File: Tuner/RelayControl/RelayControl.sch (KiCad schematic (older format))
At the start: 90 parts, among them J1 Conn_01x06, J12 Conn_01x01, J13 Conn_01x01, J14 Conn_01x01, J2 Conn_02x16_Odd_Even, J7 Conn_01x01, U1 MCP23017, U2 ULN2803A, U3 ULN2803A

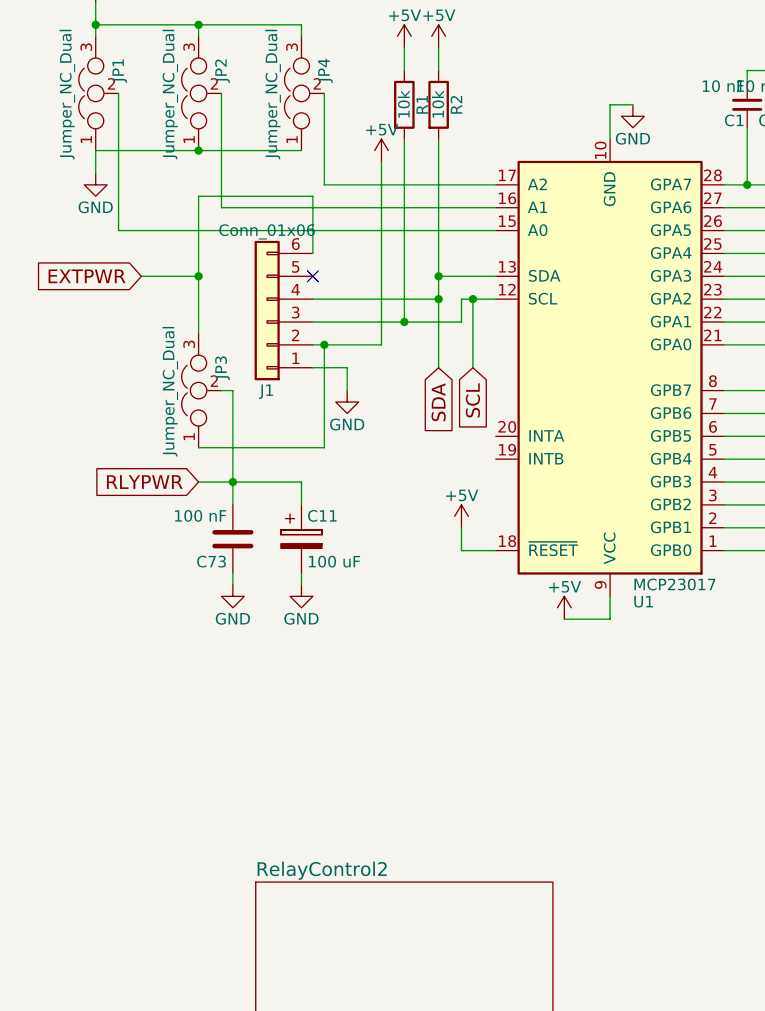
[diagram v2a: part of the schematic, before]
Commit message: JLCPCB order 09232018 - improved grounding - improved I2C cabling - NEO7M port - support for common mode chokes - relay board now has capacitors on all coils
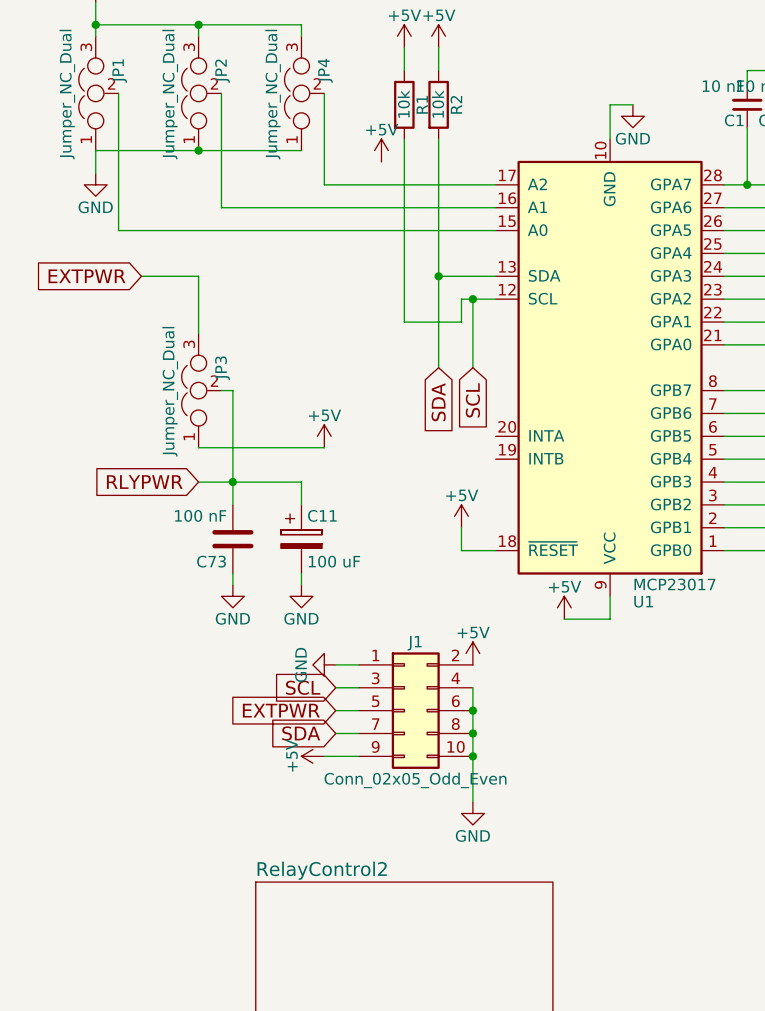
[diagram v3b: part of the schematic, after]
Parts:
- removed J1: Conn_01x06, Connectors_Molex:Molex_KK-6410-06_06x2.54mm_Straight, symbol Conn_01x06
- added J1: Conn_02x05_Odd_Even, Pin_Headers:Pin_Header_Straight_2x05_Pitch2.54mm, symbol Conn_02x05_Odd_Even
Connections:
- net +5V: now also J1.2 (Pin_2), J1.9 (Pin_9)
- net EXTPWR: now also J1.5 (Pin_5)
- net GND: now also J1.1 (Pin_1), J1.10 (Pin_10), J1.4 (Pin_4), J1.6 (Pin_6), J1.8 (Pin_8)
- net SCL: now also J1.3 (Pin_3)
- net SDA: now also J1.7 (Pin_7)
- no-connect marks 2 -> 1
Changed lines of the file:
@@
 $EndComp
 $Comp
-L +5V #PWR3
+L +5V #PWR01
 U 1 1 5B1ABFC6
 P 1050 850
-F 0 "#PWR3" H 1050 700 50  0001 C CNN
+F 0 "#PWR01" H 1050 700 50  0001 C CNN
 F 1 "+5V" H 1050 990 50  0000 C CNN
 F 2 "" H 1050 850 50  0001 C CNN
@@
 $EndComp
 $Comp
-L GND #PWR4
+L GND #PWR02
 U 1 1 5B1AC04C
 P 1050 1300
-F 0 "#PWR4" H 1050 1050 50  0001 C CNN
+F 0 "#PWR02" H 1050 1050 50  0001 C CNN
 F 1 "GND" H 1050 1150 50  0000 C CNN
 F 2 "" H 1050 1300 50  0001 C CNN
@@
 $EndComp
 $Comp
-L GND #PWR2
+L GND #PWR03
 U 1 1 5B8A6CD4
 P 900 2900
-F 0 "#PWR2" H 900 2650 50  0001 C CNN
+F 0 "#PWR03" H 900 2650 50  0001 C CNN
 F 1 "GND" H 900 2750 50  0000 C CNN
 F 2 "" H 900 2900 50  0001 C CNN
@@
 $EndComp
 $Comp
-L +5V #PWR1
+L +5V #PWR04
 U 1 1 5B8A6CDA
 P 900 2150
-F 0 "#PWR1" H 900 2000 50  0001 C CNN
+F 0 "#PWR04" H 900 2000 50  0001 C CNN
 F 1 "+5V" H 900 2290 50  0000 C CNN
 F 2 "" H 900 2150 50  0001 C CNN
@@
 $EndComp
 $Comp
-L GND #PWR7
-U 1 1 5B8A6CE0
-P 2000 3850
-F 0 "#PWR7" H 2000 3600 50  0001 C CNN
-F 1 "GND" H 2000 3700 50  0000 C CNN
-F 2 "" H 2000 3850 50  0001 C CNN
-F 3 "" H 2000 3850 50  0001 C CNN
-	1    2000 3850
-	1    0    0    -1
-$EndComp
-$Comp
-L +5V #PWR8
+L +5V #PWR05
 U 1 1 5B8A6CE6
 P 2150 2850
-F 0 "#PWR8" H 2150 2700 50  0001 C CNN
+F 0 "#PWR05" H 2150 2700 50  0001 C CNN
 F 1 "+5V" H 2150 2990 50  0000 C CNN
 F 2 "" H 2150 2850 50  0001 C CNN
@@
 $EndComp
 $Comp
-L +5V #PWR10
+L +5V #PWR06
 U 1 1 5B8A6CF2
 P 2400 2350
-F 0 "#PWR10" H 2400 2200 50  0001 C CNN
+F 0 "#PWR06" H 2400 2200 50  0001 C CNN
 F 1 "+5V" H 2400 2490 50  0000 C CNN
 F 2 "" H 2400 2350 50  0001 C CNN
@@
 $EndComp
 $Comp
-L +5V #PWR9
+L +5V #PWR07
 U 1 1 5B8A6D05
 P 2250 2350
-F 0 "#PWR9" H 2250 2200 50  0001 C CNN
+F 0 "#PWR07" H 2250 2200 50  0001 C CNN
 F 1 "+5V" H 2250 2490 50  0000 C CNN
 F 2 "" H 2250 2350 50  0001 C CNN
@@
 $EndComp
 $Comp
-L GND #PWR15
+L GND #PWR08
 U 1 1 5B8A94DA
 P 3250 2600
-F 0 "#PWR15" H 3250 2350 50  0001 C CNN
+F 0 "#PWR08" H 3250 2350 50  0001 C CNN
 F 1 "GND" H 3250 2450 50  0000 C CNN
 F 2 "" H 3250 2600 50  0001 C CNN
@@
 	1    3250 2600
 	1    0    0    -1
-$EndComp
-NoConn ~ 1850 3350
-$Comp
-L Conn_01x06 J1
-U 1 1 5B8A9DE5
-P 1650 3550
-F 0 "J1" H 1650 3850 50  0000 C CNN
-F 1 "Conn_01x06" H 1650 3150 50  0000 C CNN
-F 2 "Connectors_Molex:Molex_KK-6410-06_06x2.54mm_Straight" H 1650 3550 50  0001 C CNN
-F 3 "" H 1650 3550 50  0001 C CNN
-	1    1650 3550
-	-1   0    0    1
 $EndComp
 $Comp
@@
 RLYPWR
 $Comp
-L +5V #PWR13
+L +5V #PWR09
 U 1 1 5B8AAB56
 P 2950 4850
-F 0 "#PWR13" H 2950 4700 50  0001 C CNN
+F 0 "#PWR09" H 2950 4700 50  0001 C CNN
 F 1 "+5V" H 2950 4990 50  0000 C CNN
 F 2 "" H 2950 4850 50  0001 C CNN
@@
 NoConn ~ 7700 6400
 $Comp
-L GND #PWR6
+L GND #PWR010
 U 1 1 5B8C5113
 P 1800 4700
-F 0 "#PWR6" H 1800 4450 50  0001 C CNN
+F 0 "#PWR010" H 1800 4450 50  0001 C CNN
 F 1 "GND" H 1800 4550 50  0000 C CNN
 F 2 "" H 1800 4700 50  0001 C CNN
@@
 $EndComp
 $Comp
-L GND #PWR5
+L GND #PWR011
 U 1 1 5B8DF3BD
 P 1500 4700
-F 0 "#PWR5" H 1500 4450 50  0001 C CNN
+F 0 "#PWR011" H 1500 4450 50  0001 C CNN
 F 1 "GND" H 1500 4550 50  0000 C CNN
 F 2 "" H 1500 4700 50  0001 C CNN
@@
 $EndComp
 $Comp
-L +5V #PWR11
+L +5V #PWR012
 U 1 1 5B942BB9
 P 2500 4450
-F 0 "#PWR11" H 2500 4300 50  0001 C CNN
+F 0 "#PWR012" H 2500 4300 50  0001 C CNN
 F 1 "+5V" H 2500 4590 50  0000 C CNN
 F 2 "" H 2500 4450 50  0001 C CNN
@@
 $EndComp
 $Comp
-L GND #PWR18
+L GND #PWR013
 U 1 1 5B97EDC9
 P 8650 5450
-F 0 "#PWR18" H 8650 5200 50  0001 C CNN
+F 0 "#PWR013" H 8650 5200 50  0001 C CNN
 F 1 "GND" H 8650 5300 50  0000 C CNN
 F 2 "" H 8650 5450 50  0001 C CNN
@@
 $EndComp
 $Comp
-L GND #PWR16
+L GND #PWR014
 U 1 1 5B992951
 P 5000 2500
-F 0 "#PWR16" H 5000 2250 50  0001 C CNN
+F 0 "#PWR014" H 5000 2250 50  0001 C CNN
 F 1 "GND" H 5000 2350 50  0000 C CNN
 F 2 "" H 5000 2500 50  0001 C CNN
@@
 $EndComp
 $Comp
-L GND #PWR17
+L GND #PWR015
 U 1 1 5B998DAB
 P 6100 3900
-F 0 "#PWR17" H 6100 3650 50  0001 C CNN
+F 0 "#PWR015" H 6100 3650 50  0001 C CNN
 F 1 "GND" H 6100 3750 50  0000 C CNN
 F 2 "" H 6100 3900 50  0001 C CNN
@@
 $EndComp
 $Comp
-L GND #PWR12
+L GND #PWR016
 U 1 1 5B980926
 P 2700 1700
-F 0 "#PWR12" H 2700 1450 50  0001 C CNN
+F 0 "#PWR016" H 2700 1450 50  0001 C CNN
 F 1 "GND" H 2700 1550 50  0000 C CNN
 F 2 "" H 2700 1700 50  0001 C CNN
@@
 $EndComp
 $Comp
-L GND #PWR14
+L GND #PWR017
 U 1 1 5B980A3F
 P 3050 1700
-F 0 "#PWR14" H 3050 1450 50  0001 C CNN
+F 0 "#PWR017" H 3050 1450 50  0001 C CNN
 F 1 "GND" H 3050 1550 50  0000 C CNN
 F 2 "" H 3050 1700 50  0001 C CNN
@@
 	1500 4650 1500 4700
 Connection ~ 1500 4250
-Connection ~ 1350 3350
 Wire Wire Line
 	1100 3350 1350 3350
@@
 Wire Wire Line
 	1450 3850 1500 3850
-Connection ~ 1900 3650
 Wire Wire Line
 	1900 4100 1350 4100
 Wire Wire Line
-	1900 3650 1900 4100
-Wire Wire Line
-	1350 3000 1350 3600
-Wire Wire Line
-	1850 3000 1350 3000
-Wire Wire Line
-	1850 3250 1850 3000
+	1350 3350 1350 3600
 Connection ~ 2400 3350
 Wire Wire Line
-	2400 3450 1850 3450
-Wire Wire Line
 	2400 3350 2650 3350
-Connection ~ 2250 3550
 Wire Wire Line
 	2250 2750 2250 3550
@@
 	2500 3550 2500 3450
 Wire Wire Line
-	1850 3550 2500 3550
+	2250 3550 2500 3550
 Wire Wire Line
 	3150 2600 3250 2600
 Wire Wire Line
 	3150 2750 3150 2600
-Wire Wire Line
-	2150 3650 2150 2850
-Wire Wire Line
-	1850 3650 2150 3650
-Wire Wire Line
-	2000 3750 2000 3850
-Wire Wire Line
-	1850 3750 2000 3750
 Wire Wire Line
 	1000 3150 2650 3150
@@
 Wire Wire Line
 	2400 2750 2400 3750
-Connection ~ 2400 3450
 Wire Wire Line
 	8750 4950 8650 4950
@@
 Wire Wire Line
 	2700 1650 2700 1700
+$Comp
+L Conn_02x05_Odd_Even J1
+U 1 1 5BA44908
+P 2250 5250
+F 0 "J1" H 2300 5550 50  0000 C CNN
+F 1 "Conn_02x05_Odd_Even" H 2300 4950 50  0000 C CNN
+F 2 "Pin_Headers:Pin_Header_Straight_2x05_Pitch2.54mm" H 2250 5250 50  0001 C CNN
+F 3 "" H 2250 5250 50  0001 C CNN
+	1    2250 5250
+	1    0    0    -1
+$EndComp
+$Comp
+L +5V #PWR018
+U 1 1 5BA4504F
+P 1900 4100
+F 0 "#PWR018" H 1900 3950 50  0001 C CNN
+F 1 "+5V" H 1900 4240 50  0000 C CNN
+F 2 "" H 1900 4100 50  0001 C CNN
+F 3 "" H 1900 4100 50  0001 C CNN
+	1    1900 4100
+	1    0    0    -1
+$EndComp
+$Comp
+L GND #PWR019
+U 1 1 5BA453DE
+P 1950 5050
+F 0 "#PWR019" H 1950 4800 50  0001 C CNN
+F 1 "GND" H 1950 4900 50  0000 C CNN
+F 2 "" H 1950 5050 50  0001 C CNN
+F 3 "" H 1950 5050 50  0001 C CNN
+	1    1950 5050
+	0    1    1    0
+$EndComp
+Wire Wire Line
+	1950 5050 2050 5050
+$Comp
+L GND #PWR020
+U 1 1 5BA45766
+P 2550 5650
+F 0 "#PWR020" H 2550 5400 50  0001 C CNN
+F 1 "GND" H 2550 5500 50  0000 C CNN
+F 2 "" H 2550 5650 50  0001 C CNN
+F 3 "" H 2550 5650 50  0001 C CNN
+	1    2550 5650
+	1    0    0    -1
+$EndComp
+Wire Wire Line
+	2550 5150 2550 5650
+Connection ~ 2550 5450
+Connection ~ 2550 5350
+Connection ~ 2550 5250
+$Comp
+L +5V #PWR021
+U 1 1 5BA4625C
+P 2550 5050
+F 0 "#PWR021" H 2550 4900 50  0001 C CNN
+F 1 "+5V" H 2550 5190 50  0000 C CNN
+F 2 "" H 2550 5050 50  0001 C CNN
+F 3 "" H 2550 5050 50  0001 C CNN
+	1    2550 5050
+	1    0    0    -1
+$EndComp
+Text GLabel 1950 5150 0    60   Input ~ 0
+SCL
+Wire Wire Line
+	1950 5150 2050 5150
+Text GLabel 1950 5350 0    60   Input ~ 0
+SDA
+Wire Wire Line
+	1950 5350 2050 5350
+Text GLabel 1950 5250 0    60   Input ~ 0
+EXTPWR
+Wire Wire Line
+	1950 5250 2050 5250
+$Comp
+L +5V #PWR022
+U 1 1 5BA46E22
+P 1900 5450
+F 0 "#PWR022" H 1900 5300 50  0001 C CNN
+F 1 "+5V" H 1900 5590 50  0000 C CNN
+F 2 "" H 1900 5450 50  0001 C CNN
+F 3 "" H 1900 5450 50  0001 C CNN
+	1    1900 5450
+	0    -1   -1   0
+$EndComp
+Wire Wire Line
+	1900 5450 2050 5450
 $EndSCHEMATC

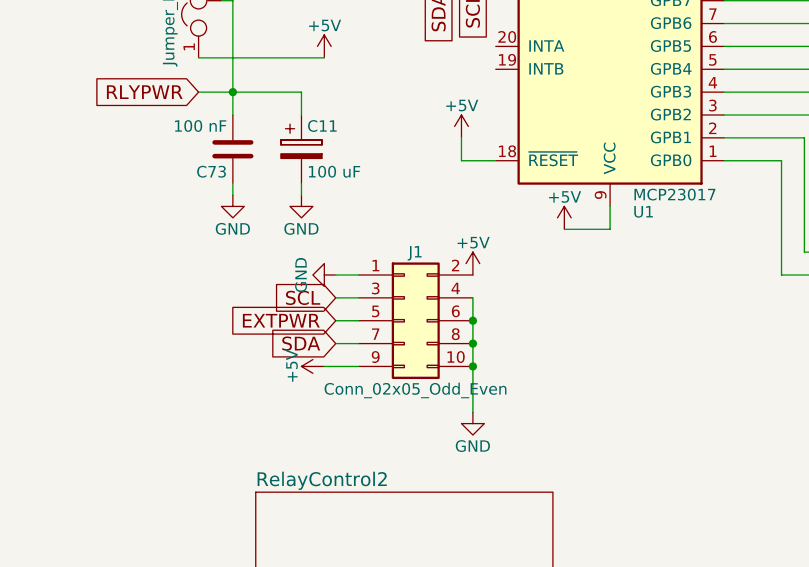
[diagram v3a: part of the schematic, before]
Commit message: Changed I2C cable pinoutgit add Tunergit add Tuner Also added ICOM rig support
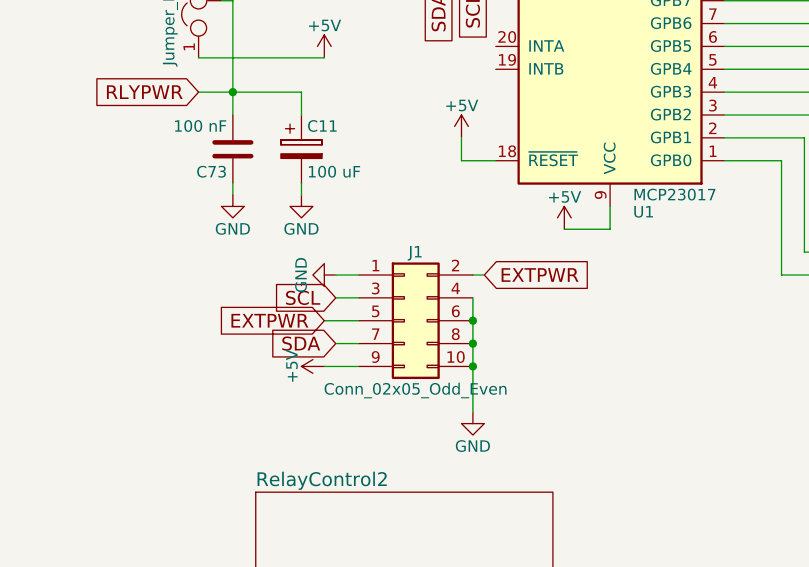
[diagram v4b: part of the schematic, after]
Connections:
- net +5V: no longer J1.2 (Pin_2)
- net EXTPWR: now also J1.2 (Pin_2)
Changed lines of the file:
@@
 Connection ~ 2550 5350
 Connection ~ 2550 5250
-$Comp
-L +5V #PWR021
-U 1 1 5BA4625C
-P 2550 5050
-F 0 "#PWR021" H 2550 4900 50  0001 C CNN
-F 1 "+5V" H 2550 5190 50  0000 C CNN
-F 2 "" H 2550 5050 50  0001 C CNN
-F 3 "" H 2550 5050 50  0001 C CNN
-	1    2550 5050
-	1    0    0    -1
-$EndComp
 Text GLabel 1950 5150 0    60   Input ~ 0
 SCL
@@
 Wire Wire Line
 	1950 5350 2050 5350
-Text GLabel 1950 5250 0    60   Input ~ 0
+Text GLabel 2600 5050 2    60   Input ~ 0
 EXTPWR
 Wire Wire Line
-	1950 5250 2050 5250
+	1900 5250 2050 5250
 $Comp
-L +5V #PWR022
+L +5V #PWR021
 U 1 1 5BA46E22
 P 1900 5450
-F 0 "#PWR022" H 1900 5300 50  0001 C CNN
+F 0 "#PWR021" H 1900 5300 50  0001 C CNN
 F 1 "+5V" H 1900 5590 50  0000 C CNN
 F 2 "" H 1900 5450 50  0001 C CNN
@@
 Wire Wire Line
 	1900 5450 2050 5450
+Wire Wire Line
+	2600 5050 2550 5050
+Text GLabel 1900 5250 0    60   Input ~ 0
+EXTPWR
 $EndSCHEMATC
